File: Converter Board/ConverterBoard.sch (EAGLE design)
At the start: 5 parts, among them P1 39-30-06, P2 39-30-06

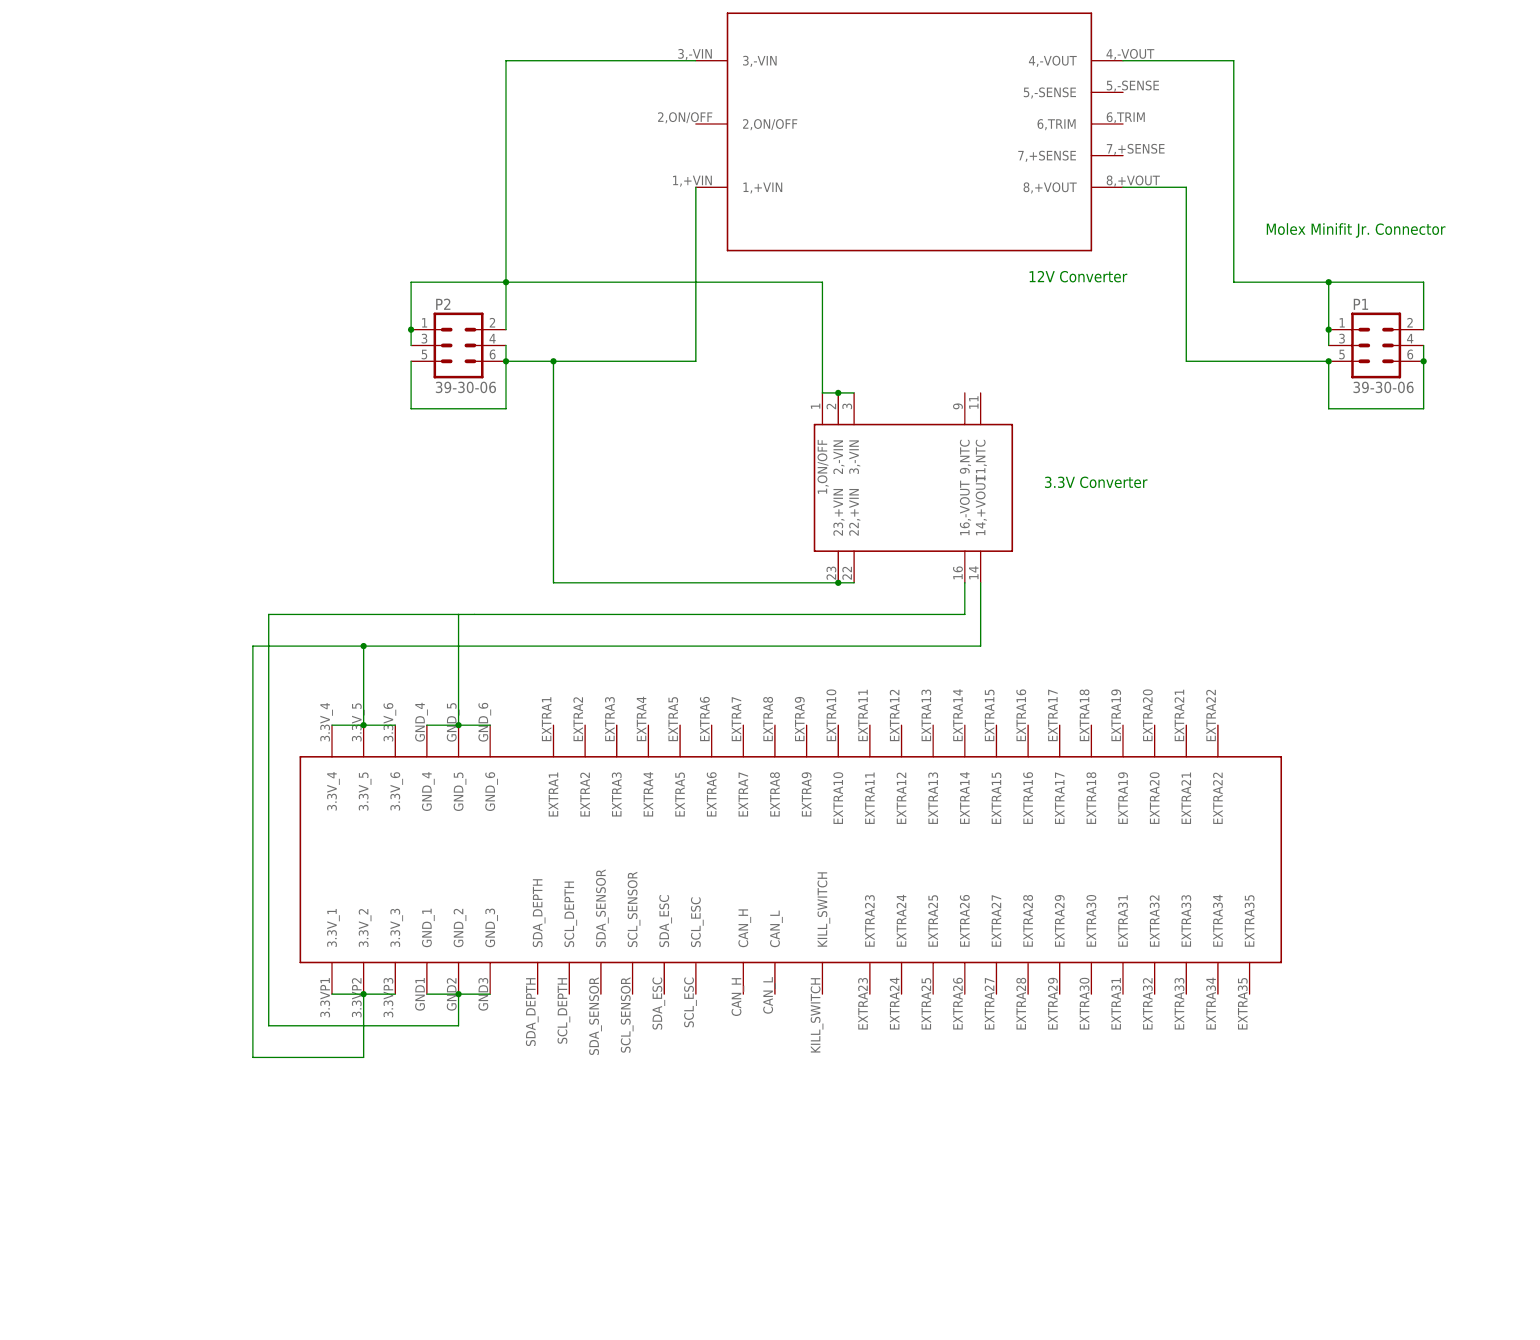
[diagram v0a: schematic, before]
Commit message: Revised 12 V and 3.3 V Converters Finished the majority of the converter board
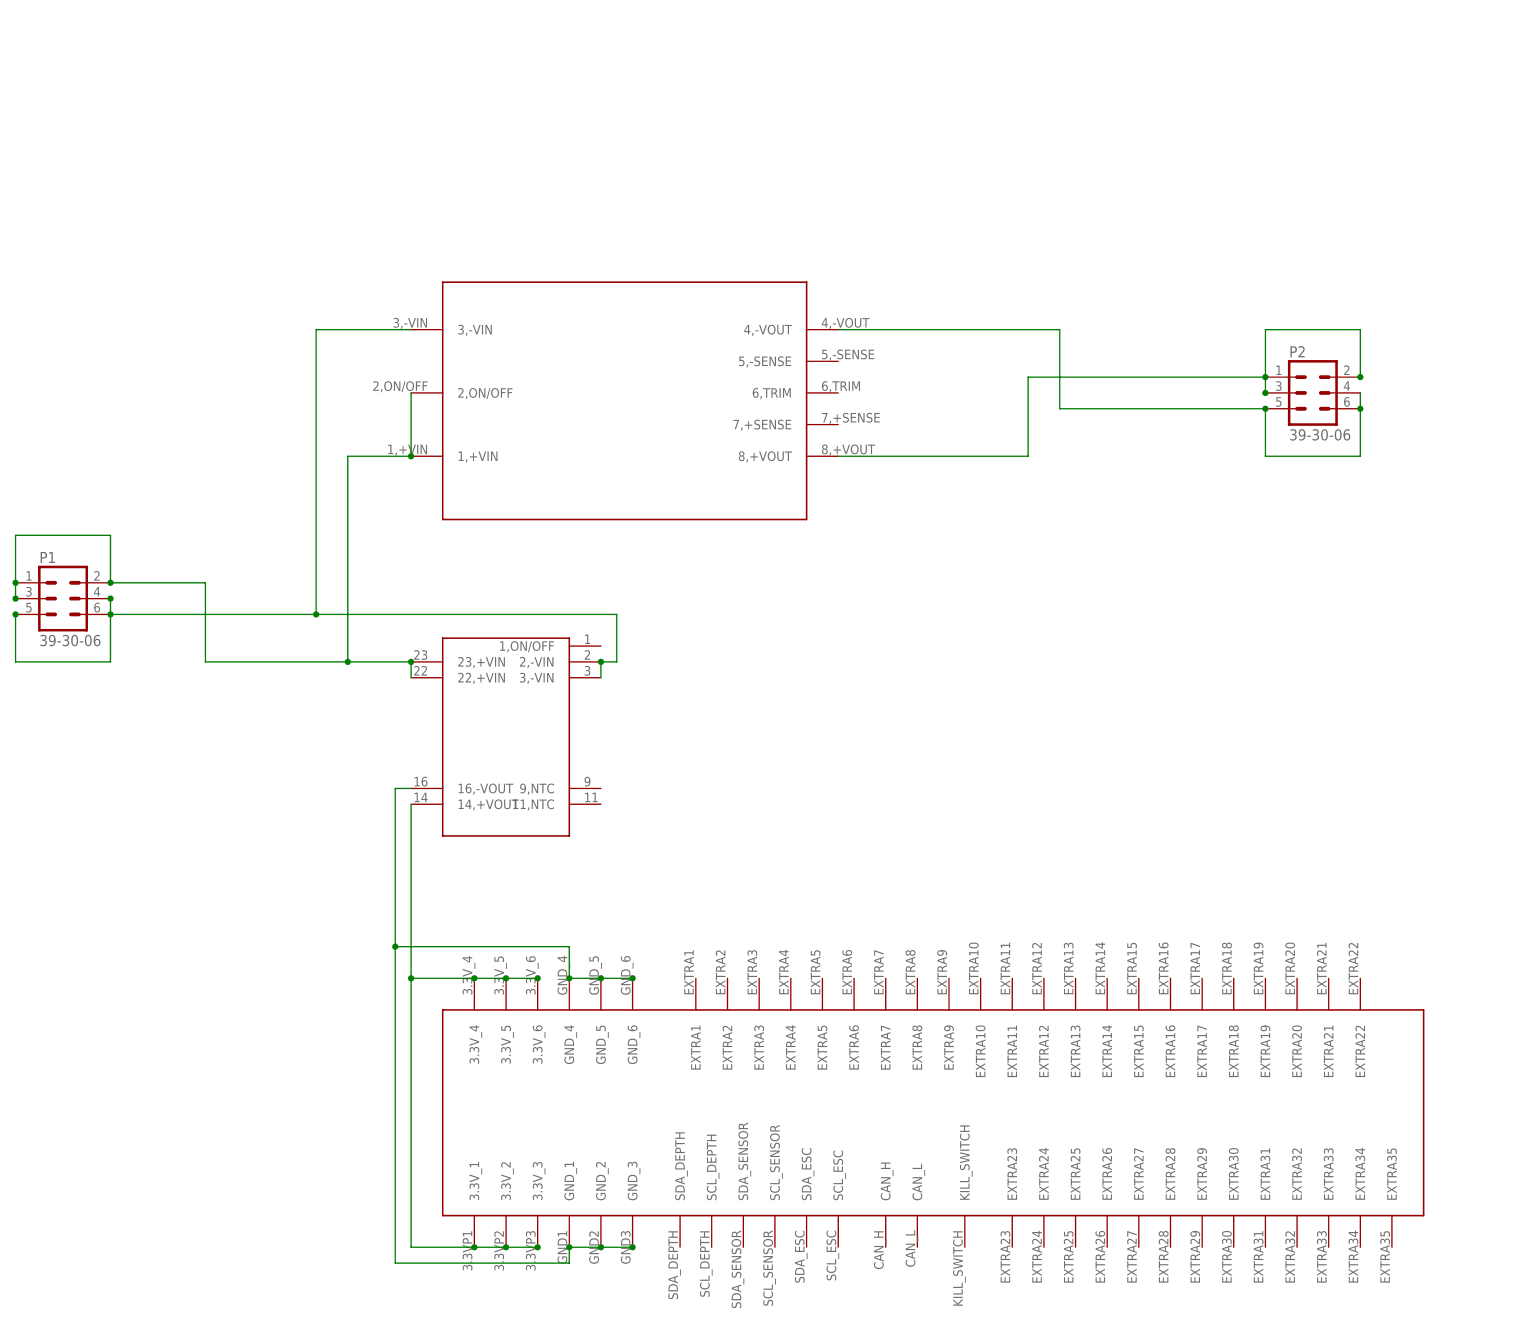
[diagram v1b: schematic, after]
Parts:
- removed U$4: 5530843, 5530843-6:5530843
- added U$3: 5530843, 5530843-6:5530843
- U$1: value 3.3VCONV -> 12VCONV; device 3.3V Converter:3.3VCONV -> 12VCONV:12VCONV
- U$2: value 12VCONV -> 3.3VCONV; device 12VCONV:12VCONV -> 3.3V Converter:3.3VCONV
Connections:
- removed net N$1: P2.4, P2.5, P2.6, U$1.22,+VIN, U$1.23,+VIN, U$2.1,+VIN
- removed net N$10: P1.1, P1.2, P1.3
- removed net N$11: P1.4, P1.5, P1.6, U$2.8,+VOUT
- removed net N$3: U$1.14,+VOUT, U$4.3.3V_1, U$4.3.3V_3, U$4.3.3V_4, U$4.3.3V_6
- removed net N$4: P2.1, P2.2, P2.3, U$1.2,-VIN, U$1.3,-VIN, U$2.3,-VIN
- removed net N$7: U$1.16,-VOUT, U$4.GND_1, U$4.GND_3, U$4.GND_4, U$4.GND_6
- new net 12V+: P2.1, P2.2, P2.3, U$1.8,+VOUT
- new net 12V-: P2.4, P2.5, P2.6, U$1.4,-VOUT
- new net 3.3V: U$2.14,+VOUT, U$3.3.3V_1, U$3.3.3V_2, U$3.3.3V_3, U$3.3.3V_4, U$3.3.3V_5, U$3.3.3V_6
- new net 3.3VGROUND: U$2.16,-VOUT, U$3.GND_1, U$3.GND_2, U$3.GND_3, U$3.GND_4, U$3.GND_5, U$3.GND_6
- new net BALANCEDRAW+: P1.1, P1.2, P1.3, U$1.1,+VIN, U$1.2,ON/OFF, U$2.22,+VIN, U$2.23,+VIN
- new net BALANCEDRAW-: P1.4, P1.5, P1.6, U$1.3,-VIN, U$2.2,-VIN, U$2.3,-VIN
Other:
- note removed: "12V Converter"
- note removed: "3.3V Converter"
- note removed: "Molex Minifit Jr. Connector"
- moved on the sheet: P1, P2

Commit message: Added LEDs and resistors to converter board
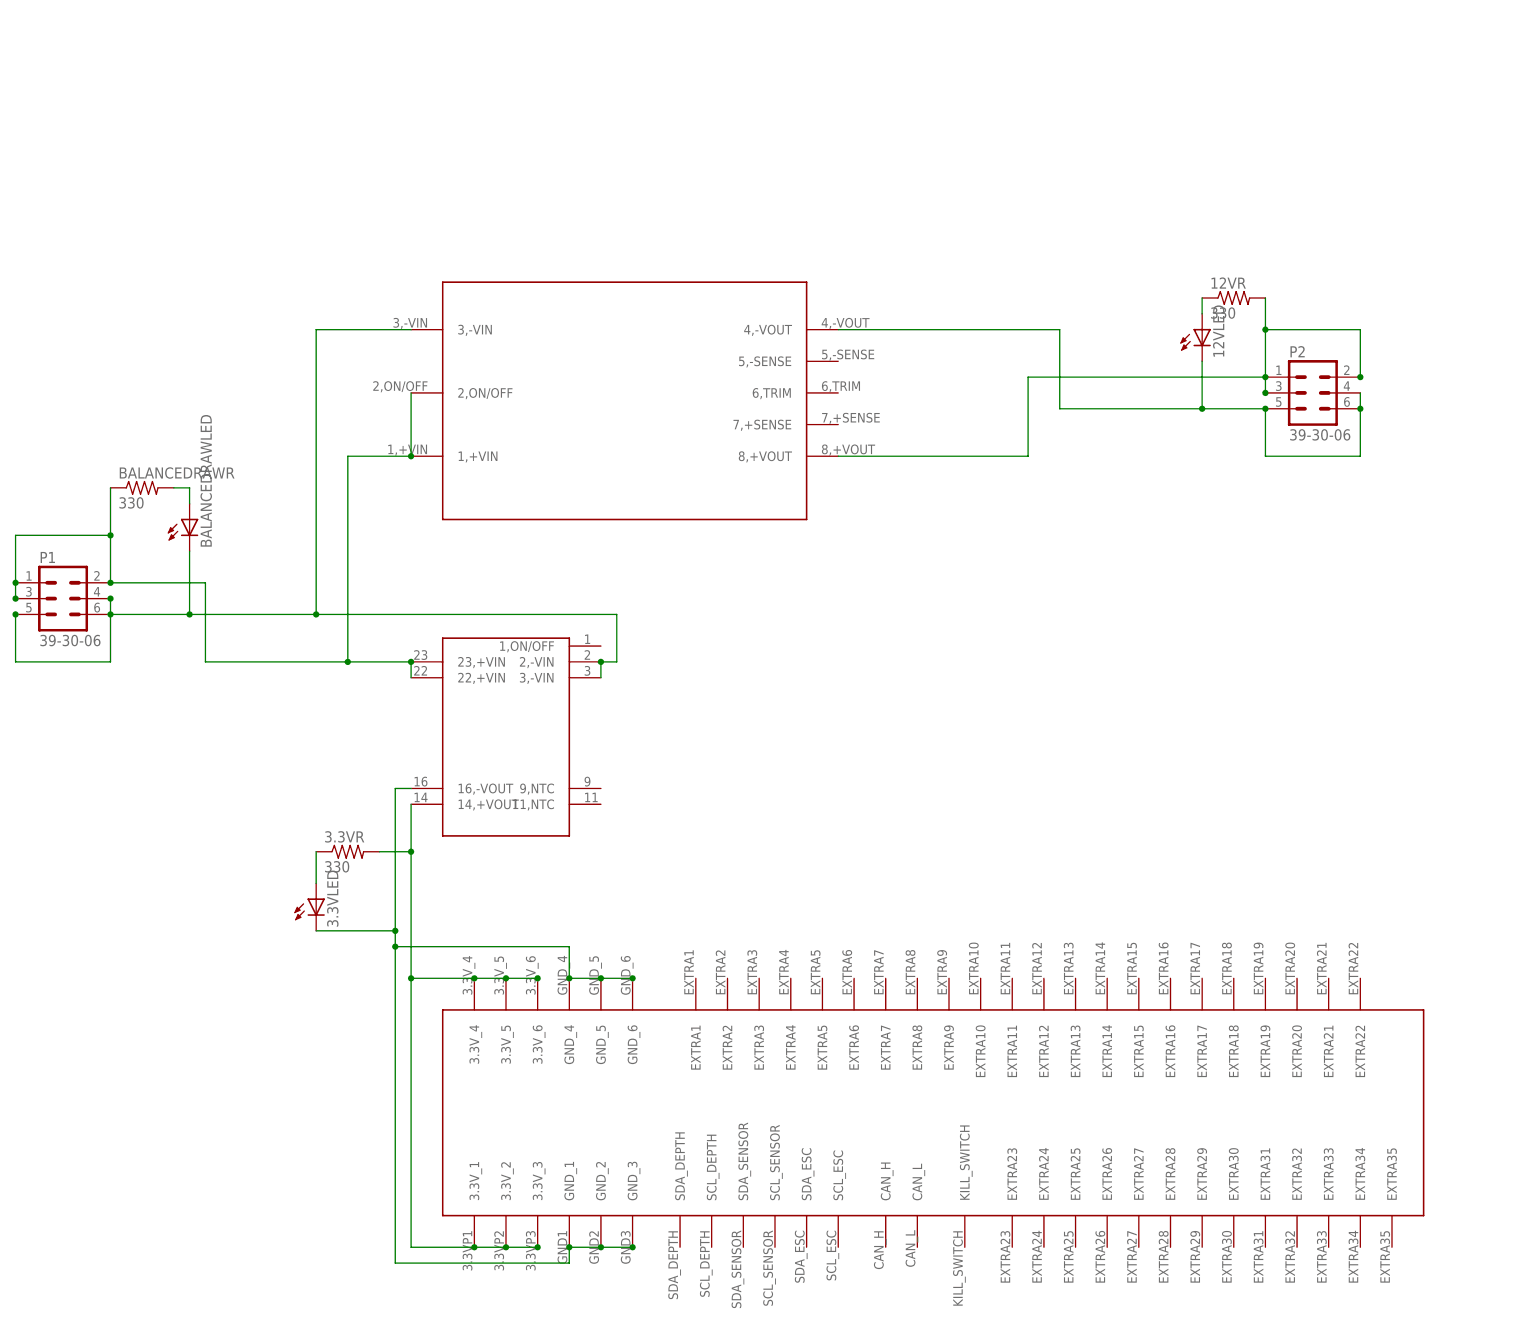
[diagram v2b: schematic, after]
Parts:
- added 12VLED, 3.3VLED, BALANCEDRAWLED: LTST-S270GKT, LTST-S270GKT:LTST-S270GKT
- added 12VR, 3.3VR, BALANCEDRAWR: 330, resistor:R-US_0204/7
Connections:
- new net 12VLED: 12VLED.A, 12VR.1
- new net 3.3VLED: 3.3VLED.A, 3.3VR.1
- new net BALANCEDRAWLED: BALANCEDRAWLED.A, BALANCEDRAWR.2
- net 12V+: now also 12VR.2
- net 12V-: now also 12VLED.C
- net 3.3V: now also 3.3VR.2
- net 3.3VGROUND: now also 3.3VLED.C
- net BALANCEDRAW+: now also BALANCEDRAWR.1
- net BALANCEDRAW-: now also BALANCEDRAWLED.C
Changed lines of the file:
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@@
 <layer number="97" name="Info" color="7" fill="1" visible="yes" active="yes"/>
 <layer number="98" name="Guide" color="6" fill="1" visible="yes" active="yes"/>
+<layer number="99" name="SpiceOrder" color="5" fill="1" visible="yes" active="yes"/>
 </layers>
 <schematic xreflabel="%F%N/%S.%C%R" xrefpart="/%S.%C%R">
@@
 <part name="U$1" library="12VCONV" deviceset="12VCONV" device=""/>
 <part name="U$2" library="3.3V Converter" deviceset="3.3VCONV" device=""/>
+<part name="3.3VLED" library="LTST-S270GKT" deviceset="LTST-S270GKT" device=""/>
+<part name="12VLED" library="LTST-S270GKT" deviceset="LTST-S270GKT" device=""/>
+<part name="BALANCEDRAWLED" library="LTST-S270GKT" deviceset="LTST-S270GKT" device=""/>
+<part name="3.3VR" library="resistor" library_urn="urn:adsk.eagle:library:348" deviceset="R-US_" device="0204/7" package3d_urn="urn:adsk.eagle:package:25945/1" value="330"/>
+<part name="BALANCEDRAWR" library="resistor" library_urn="urn:adsk.eagle:library:348" deviceset="R-US_" device="0204/7" package3d_urn="urn:adsk.eagle:package:25945/1" value="330"/>
+<part name="12VR" library="resistor" library_urn="urn:adsk.eagle:library:348" deviceset="R-US_" device="0204/7" package3d_urn="urn:adsk.eagle:package:25945/1" value="330"/>
 </parts>
 <sheets>
@@
 <instance part="U$1" gate="G$1" x="0" y="58.42"/>
 <instance part="U$2" gate="G$1" x="0" y="7.62"/>
+<instance part="3.3VLED" gate="G$1" x="-20.32" y="-2.54"/>
+<instance part="12VLED" gate="G$1" x="121.92" y="88.9"/>
+<instance part="BALANCEDRAWLED" gate="G$1" x="-40.64" y="58.42"/>
+<instance part="3.3VR" gate="G$1" x="-15.24" y="5.08"/>
+<instance part="BALANCEDRAWR" gate="G$1" x="-48.26" y="63.5"/>
+<instance part="12VR" gate="G$1" x="127" y="93.98"/>
 </instances>
 <busses>
@@
 <pinref part="U$2" gate="G$1" pin="23,+VIN"/>
 <junction x="-5.08" y="35.56"/>
+<pinref part="BALANCEDRAWR" gate="G$1" pin="1"/>
+<wire x1="-53.34" y1="55.88" x2="-53.34" y2="63.5" width="0.1524" layer="91"/>
+<junction x="-53.34" y="55.88"/>
 </segment>
 </net>
@@
 <wire x1="-53.34" y1="45.72" x2="-53.34" y2="43.18" width="0.1524" layer="91"/>
 <junction x="-53.34" y="45.72"/>
-<wire x1="-53.34" y1="43.18" x2="-20.32" y2="43.18" width="0.1524" layer="91"/>
+<wire x1="-53.34" y1="43.18" x2="-40.64" y2="43.18" width="0.1524" layer="91"/>
+<wire x1="-40.64" y1="43.18" x2="-20.32" y2="43.18" width="0.1524" layer="91"/>
 <wire x1="-20.32" y1="43.18" x2="27.94" y2="43.18" width="0.1524" layer="91"/>
 <wire x1="-5.08" y1="88.9" x2="-20.32" y2="88.9" width="0.1524" layer="91"/>
@@
 <junction x="25.4" y="35.56"/>
 <pinref part="U$2" gate="G$1" pin="3,-VIN"/>
+<pinref part="BALANCEDRAWLED" gate="G$1" pin="C"/>
+<wire x1="-40.64" y1="53.34" x2="-40.64" y2="43.18" width="0.1524" layer="91"/>
+<junction x="-40.64" y="43.18"/>
 </segment>
 </net>
@@
 <wire x1="63.5" y1="88.9" x2="99.06" y2="88.9" width="0.1524" layer="91"/>
 <wire x1="99.06" y1="88.9" x2="99.06" y2="76.2" width="0.1524" layer="91"/>
-<wire x1="99.06" y1="76.2" x2="132.08" y2="76.2" width="0.1524" layer="91"/>
+<wire x1="99.06" y1="76.2" x2="121.92" y2="76.2" width="0.1524" layer="91"/>
 <pinref part="U$1" gate="G$1" pin="4,-VOUT"/>
+<pinref part="12VLED" gate="G$1" pin="C"/>
+<wire x1="121.92" y1="76.2" x2="132.08" y2="76.2" width="0.1524" layer="91"/>
+<wire x1="121.92" y1="83.82" x2="121.92" y2="76.2" width="0.1524" layer="91"/>
+<junction x="121.92" y="76.2"/>
 </segment>
 </net>
@@
 <wire x1="5.08" y1="-58.42" x2="10.16" y2="-58.42" width="0.1524" layer="91"/>
 <wire x1="10.16" y1="-58.42" x2="15.24" y2="-58.42" width="0.1524" layer="91"/>
-<wire x1="-5.08" y1="12.7" x2="-5.08" y2="-15.24" width="0.1524" layer="91"/>
+<wire x1="-5.08" y1="12.7" x2="-5.08" y2="5.08" width="0.1524" layer="91"/>
+<wire x1="-5.08" y1="5.08" x2="-5.08" y2="-15.24" width="0.1524" layer="91"/>
 <wire x1="-5.08" y1="-15.24" x2="-5.08" y2="-58.42" width="0.1524" layer="91"/>
 <wire x1="-5.08" y1="-58.42" x2="5.08" y2="-58.42" width="0.1524" layer="91"/>
@@
 <junction x="15.24" y="-58.42"/>
 <pinref part="U$2" gate="G$1" pin="14,+VOUT"/>
+<pinref part="3.3VR" gate="G$1" pin="2"/>
+<wire x1="-10.16" y1="5.08" x2="-5.08" y2="5.08" width="0.1524" layer="91"/>
+<junction x="-5.08" y="5.08"/>
 </segment>
 </net>
@@
 <wire x1="25.4" y1="-15.24" x2="20.32" y2="-15.24" width="0.1524" layer="91"/>
 <wire x1="-5.08" y1="15.24" x2="-7.62" y2="15.24" width="0.1524" layer="91"/>
-<wire x1="-7.62" y1="15.24" x2="-7.62" y2="-10.16" width="0.1524" layer="91"/>
+<wire x1="-7.62" y1="15.24" x2="-7.62" y2="-7.62" width="0.1524" layer="91"/>
+<wire x1="-7.62" y1="-7.62" x2="-7.62" y2="-10.16" width="0.1524" layer="91"/>
 <wire x1="-7.62" y1="-10.16" x2="20.32" y2="-10.16" width="0.1524" layer="91"/>
 <wire x1="20.32" y1="-10.16" x2="20.32" y2="-15.24" width="0.1524" layer="91"/>
@@
 <junction x="30.48" y="-15.24"/>
 <pinref part="U$2" gate="G$1" pin="16,-VOUT"/>
+<pinref part="3.3VLED" gate="G$1" pin="C"/>
+<wire x1="-20.32" y1="-7.62" x2="-7.62" y2="-7.62" width="0.1524" layer="91"/>
+<junction x="-7.62" y="-7.62"/>
 </segment>
 </net>
@@
 <wire x1="93.98" y1="81.28" x2="132.08" y2="81.28" width="0.1524" layer="91"/>
 <pinref part="U$1" gate="G$1" pin="8,+VOUT"/>
+<pinref part="12VR" gate="G$1" pin="2"/>
+<wire x1="132.08" y1="88.9" x2="132.08" y2="93.98" width="0.1524" layer="91"/>
+<junction x="132.08" y="88.9"/>
+</segment>
+</net>
+<net name="3.3VLED" class="0">
+<segment>
+<pinref part="3.3VR" gate="G$1" pin="1"/>
+<pinref part="3.3VLED" gate="G$1" pin="A"/>
+<wire x1="-20.32" y1="5.08" x2="-20.32" y2="0" width="0.1524" layer="91"/>
+</segment>
+</net>
+<net name="BALANCEDRAWLED" class="0">
+<segment>
+<pinref part="BALANCEDRAWR" gate="G$1" pin="2"/>
+<pinref part="BALANCEDRAWLED" gate="G$1" pin="A"/>
+<wire x1="-43.18" y1="63.5" x2="-40.64" y2="63.5" width="0.1524" layer="91"/>
+<wire x1="-40.64" y1="63.5" x2="-40.64" y2="60.96" width="0.1524" layer="91"/>
+</segment>
+</net>
+<net name="12VLED" class="0">
+<segment>
+<pinref part="12VR" gate="G$1" pin="1"/>
+<pinref part="12VLED" gate="G$1" pin="A"/>
+<wire x1="121.92" y1="93.98" x2="121.92" y2="91.44" width="0.1524" layer="91"/>
 </segment>
 </net>
@@
 </schematic>
 </drawing>
+<compatibility>
+<note version="8.2" severity="warning">
+Since Version 8.2, EAGLE supports online libraries. The ids
+of those online libraries will not be understood (or retained)
+with this version.
+</note>
+<note version="8.3" severity="warning">
+Since Version 8.3, EAGLE supports URNs for individual library
+assets (packages, symbols, and devices). The URNs of those assets
+will not be understood (or retained) with this version.
+</note>
+<note version="8.3" severity="warning">
+Since Version 8.3, EAGLE supports the association of 3D packages
+with devices in libraries, schematics, and board files. Those 3D
+packages will not be understood (or retained) with this version.
+</note>
+</compatibility>
 </eagle>
